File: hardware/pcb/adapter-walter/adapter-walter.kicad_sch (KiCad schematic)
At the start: 4 parts, among them U1 DPT_Walter

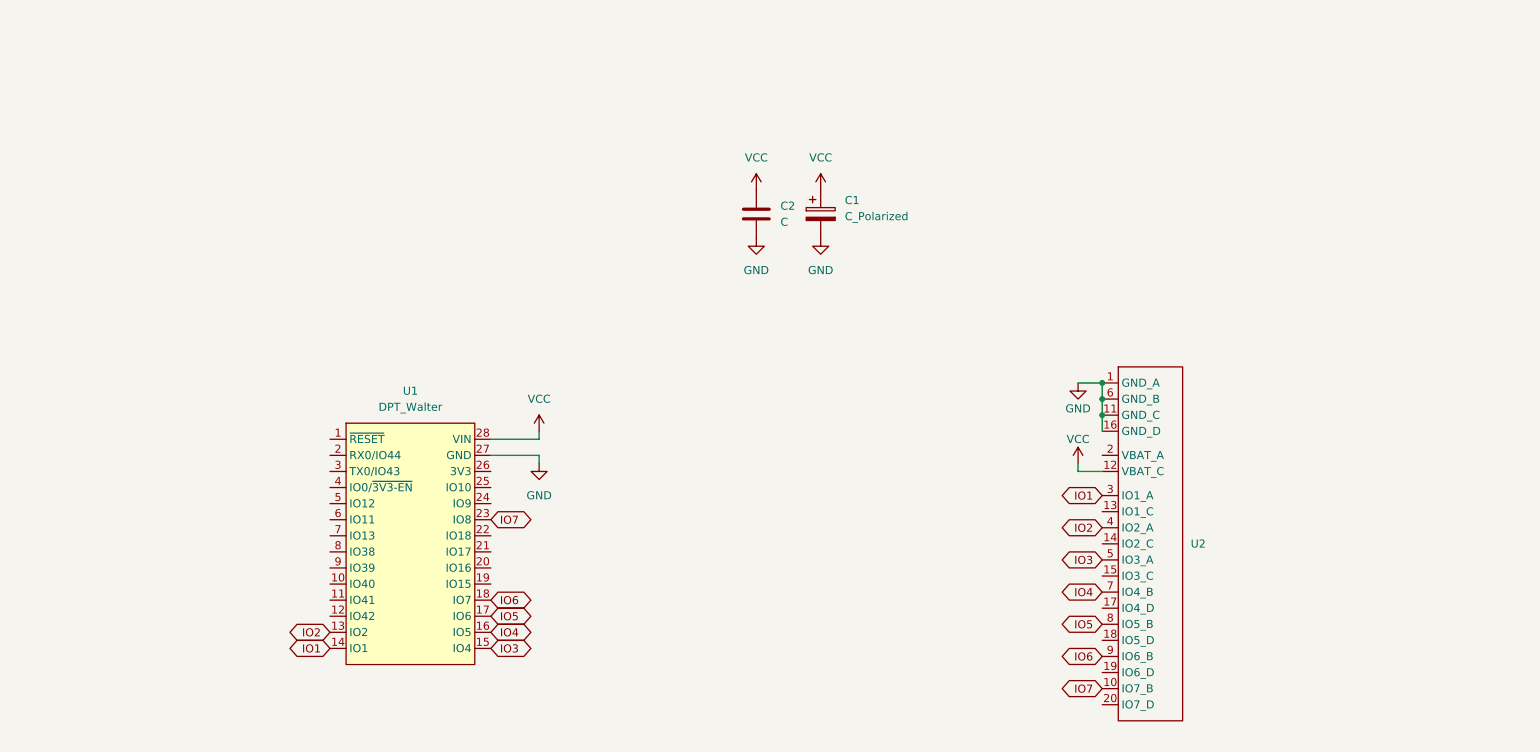
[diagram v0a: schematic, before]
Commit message: Updated Walter adapter schematics
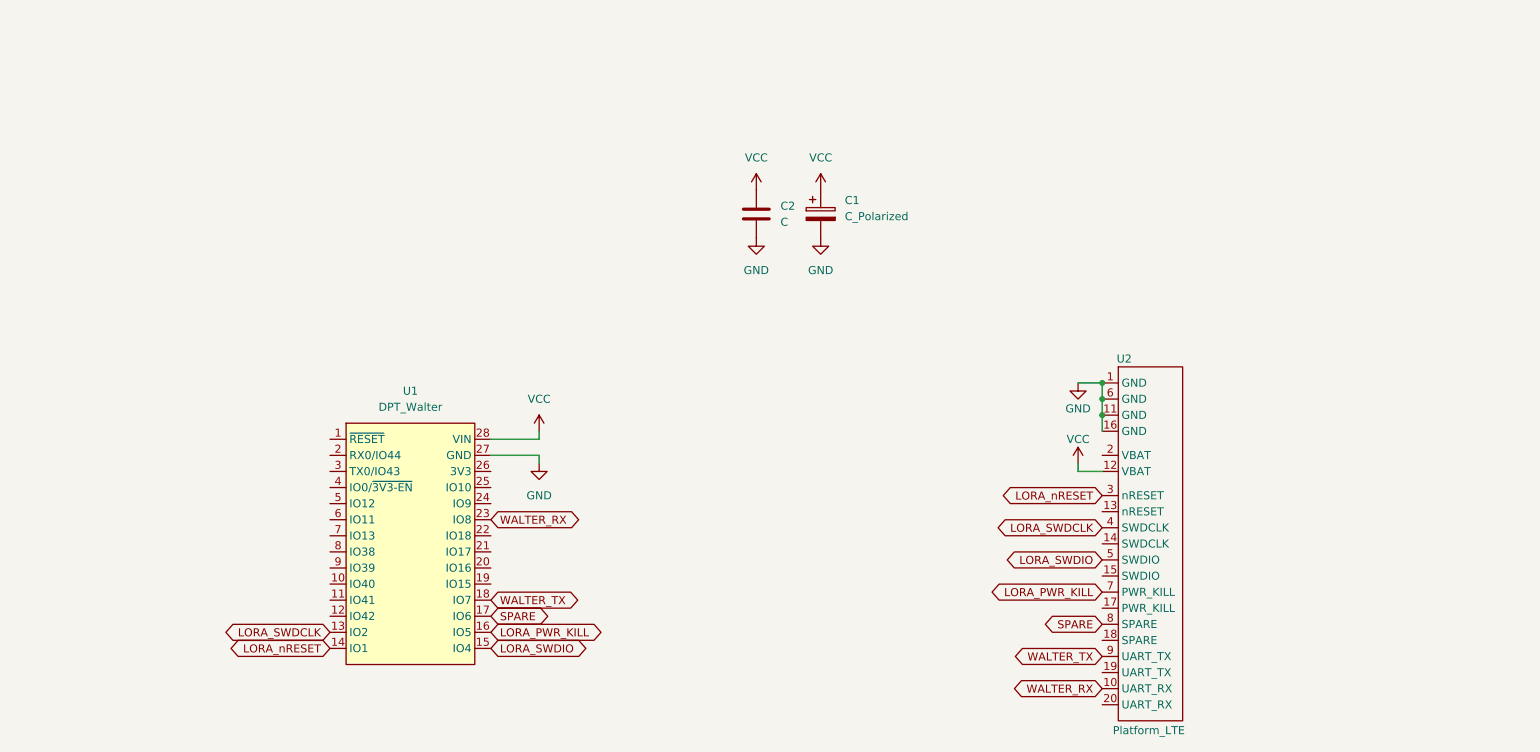
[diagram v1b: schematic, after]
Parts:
- U2: value (none) -> Platform_LTE; symbol TwinOak-standard-repeater-layout:Platform_interface -> TwinOak-standard-repeater-layout:Platform_LTE
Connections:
- net IO1 renamed LORA_nRESET
- net IO2 renamed LORA_SWDCLK
- net IO3 renamed LORA_SWDIO
- net IO4 renamed LORA_PWR_KILL
- net IO5 renamed SPARE
- net IO6 renamed WALTER_TX
- net IO7 renamed WALTER_RX
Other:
- moved on the sheet: U2
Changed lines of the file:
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@@
 		)
 	)
-	(global_label "IO4"
+	(global_label "LORA_PWR_KILL"
 		(shape bidirectional)
 		(at 106.68 118.11 0)
@@
 		)
 	)
-	(global_label "IO7"
+	(global_label "WALTER_RX"
 		(shape bidirectional)
 		(at 106.68 100.33 0)
@@
 		)
 	)
-	(global_label "IO6"
+	(global_label "WALTER_TX"
 		(shape bidirectional)
 		(at 203.2 121.92 180)
@@
 		)
 	)
-	(global_label "IO2"
+	(global_label "LORA_SWDCLK"
 		(shape bidirectional)
 		(at 81.28 118.11 180)
@@
 		)
 	)
-	(global_label "IO1"
+	(global_label "LORA_nRESET"
 		(shape bidirectional)
 		(at 81.28 120.65 180)
@@
 		)
 	)
-	(global_label "IO3"
+	(global_label "LORA_SWDIO"
 		(shape bidirectional)
 		(at 203.2 106.68 180)
@@
 		)
 	)
-	(global_label "IO5"
+	(global_label "SPARE"
 		(shape bidirectional)
 		(at 106.68 115.57 0)
@@
 		)
 	)
-	(global_label "IO6"
+	(global_label "WALTER_TX"
 		(shape bidirectional)
 		(at 106.68 113.03 0)
@@
 		)
 	)
-	(global_label "IO3"
+	(global_label "LORA_SWDIO"
 		(shape bidirectional)
 		(at 106.68 120.65 0)
@@
 		)
 	)
-	(global_label "IO7"
+	(global_label "WALTER_RX"
 		(shape bidirectional)
 		(at 203.2 127 180)
@@
 		)
 	)
-	(global_label "IO1"
+	(global_label "LORA_nRESET"
 		(shape bidirectional)
 		(at 203.2 96.52 180)
@@
 		)
 	)
-	(global_label "IO4"
+	(global_label "LORA_PWR_KILL"
 		(shape bidirectional)
 		(at 203.2 111.76 180)
@@
 		)
 	)
-	(global_label "IO5"
+	(global_label "SPARE"
 		(shape bidirectional)
 		(at 203.2 116.84 180)
@@
 		)
 	)
-	(global_label "IO2"
+	(global_label "LORA_SWDCLK"
 		(shape bidirectional)
 		(at 203.2 101.6 180)
@@
 	)
 	(symbol
-		(lib_id "TwinOak-standard-repeater-layout:Platform_interface")
+		(lib_id "TwinOak-standard-repeater-layout:Platform_LTE")
 		(at 205.74 76.2 0)
 		(unit 1)
@@
 		(in_pos_files yes)
 		(dnp no)
-		(fields_autoplaced yes)
 		(property "Reference" "U2"
-			(at 217.17 104.1399 0)
+			(at 205.486 74.93 0)
 			(show_name no)
 			(do_not_autoplace no)
@@
 			)
 		)
-		(property "Value" ""
-			(at 205.74 76.2 0)
-			(show_name no)
-			(do_not_autoplace no)
+		(property "Value" "Platform_LTE"
+			(at 210.566 133.604 0)
+			(show_name no)
+			(do_not_autoplace no)

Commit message: Cleanup
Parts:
- added SW1: RESET, TwinOak:SW_Push_Kinghelm_KH-6X6X5H-STM, symbol Switch:SW_Push
- C1: value C_Polarized -> 470u 16V; MPN (none) -> Panasonic 16SEPG470M (OS-CON)
- C2: value C -> 10n; MPN (none) -> SR Passives CCT-10N/100V-S
- U1: footprint walter:walter-socket -> TwinOak:walter-socket; symbol walter:DPT_Walter -> TwinOak:DPT_Walter
- U2: footprint TwinOak platform footprints:platform-adapter-footprint -> TwinOak:platform-adapter-footprint; symbol TwinOak-standard-repeater-layout:Platform_LTE -> TwinOak:Platform_LTE
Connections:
- net GND: now also SW1.1
- net WALTER_nRST: now reaches U1.1 (~{RESET})
- net WALTER_nRST: now also SW1.2
- no-connect marks 0 -> 26

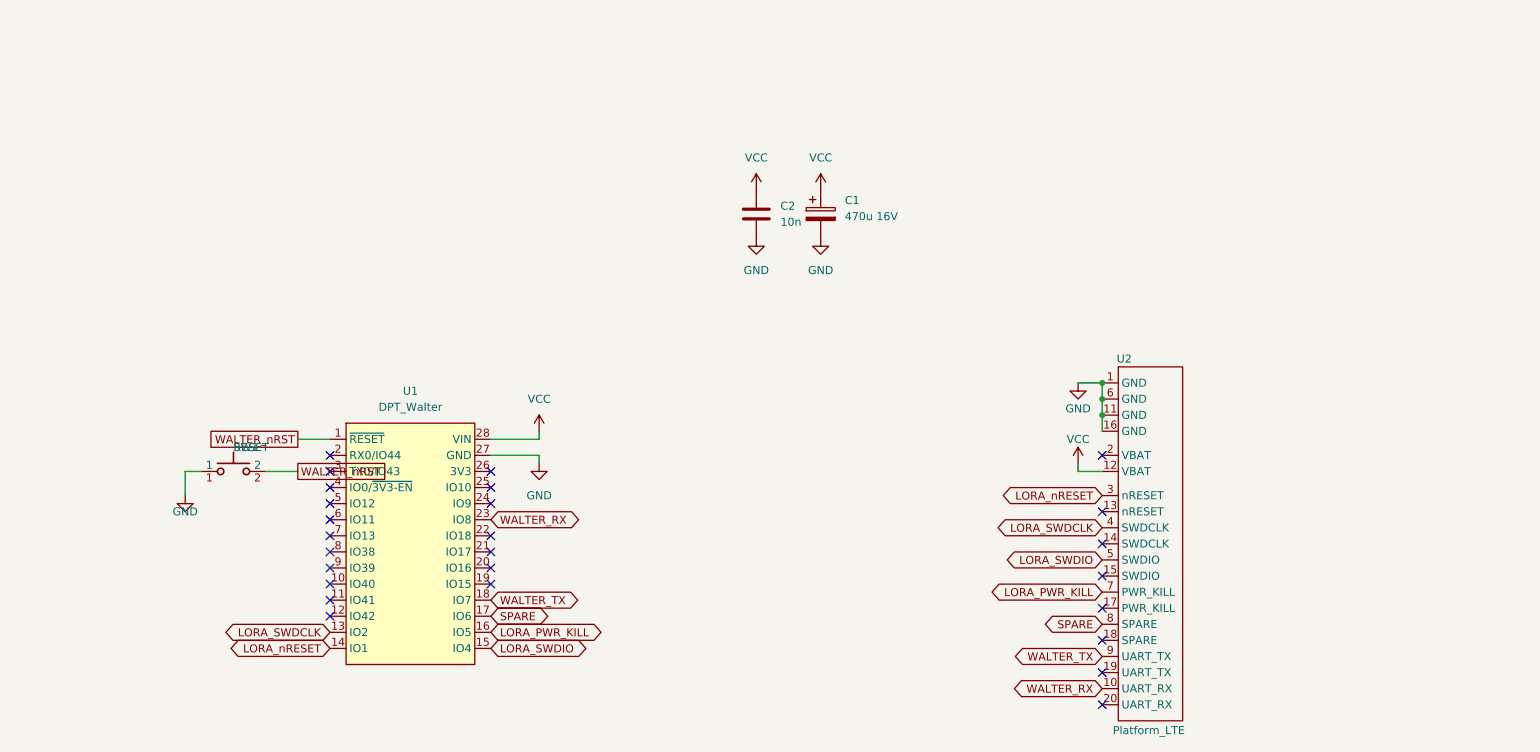
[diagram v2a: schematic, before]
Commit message: Cleanup. Added feedback prevention circuits to Walter adapter
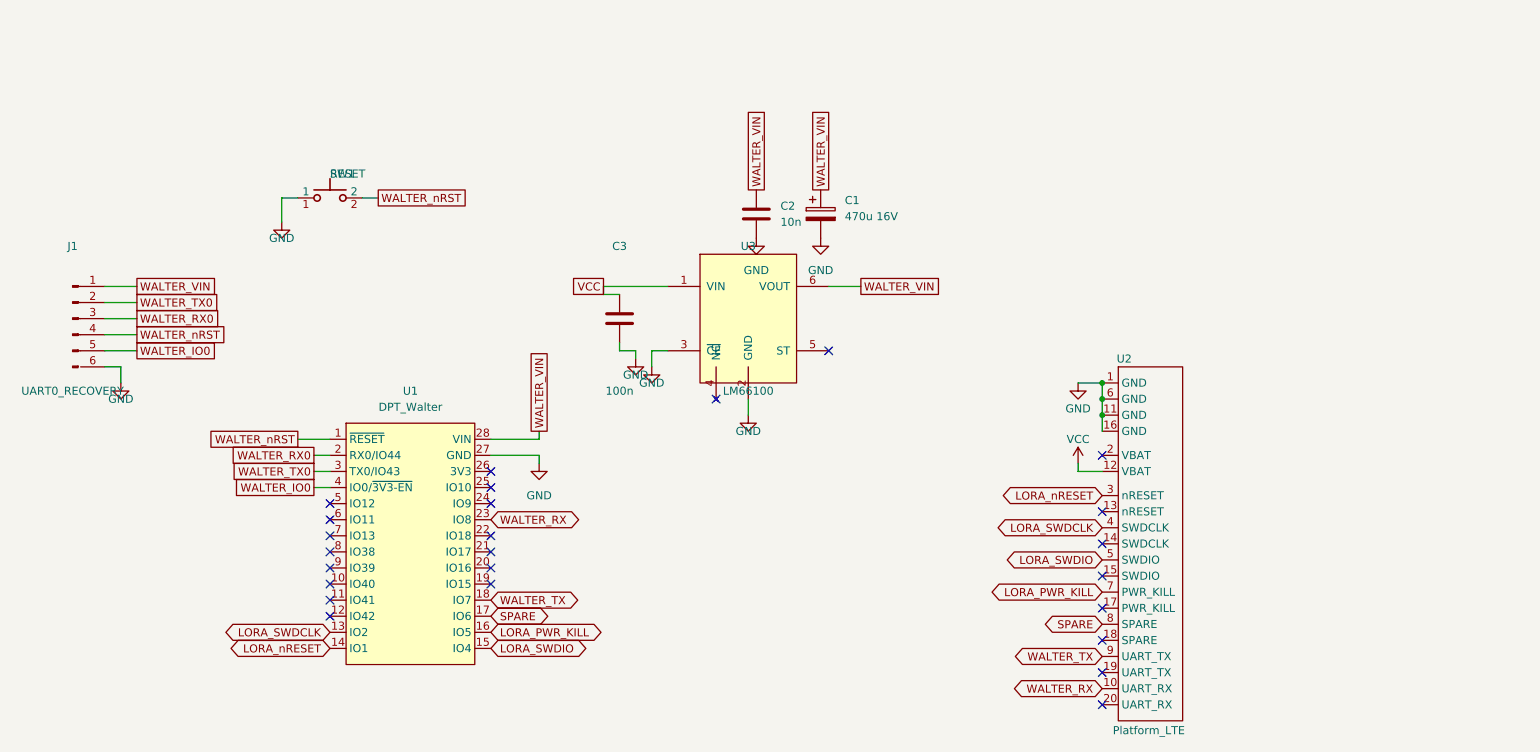
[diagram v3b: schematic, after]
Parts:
- added C3: 100n, Capacitor_SMD:C_0805_2012Metric_Pad1.18x1.45mm_HandSolder, symbol Device:C
- added J1: UART0_RECOVERY, Connector_PinHeader_2.54mm:PinHeader_1x06_P2.54mm_Vertical, symbol Connector:Conn_01x06_Pin
- added U3: LM66100, Package_TO_SOT_SMD:SOT-363_SC-70-6, symbol TwinOak:LM66100
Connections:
- net GND: now also C3.2, J1.6 (Pin_6), U3.2 (GND), U3.3 (~{CE})
- net VCC: now also C3.1, U3.1 (VIN); no longer C1.1, C2.1, U1.28 (VIN)
- net WALTER_nRST: now also J1.4 (Pin_4)
- net WALTER_RX0: now reaches U1.2 (RX0/IO44)
- net WALTER_RX0: now also J1.3 (Pin_3)
- net WALTER_TX0: now reaches U1.3 (TX0/IO43)
- net WALTER_TX0: now also J1.2 (Pin_2)
- net WALTER_IO0: now reaches U1.4 (IO0/~{3V3-EN})
- net WALTER_IO0: now also J1.5 (Pin_5)
- new net WALTER_VIN: C1.1, C2.1, J1.1 (Pin_1), U1.28 (VIN), U3.6 (VOUT)
- no-connect marks 26 -> 25
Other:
- moved on the sheet: SW1

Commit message: Initial routing of walter - Not finished, missing polish
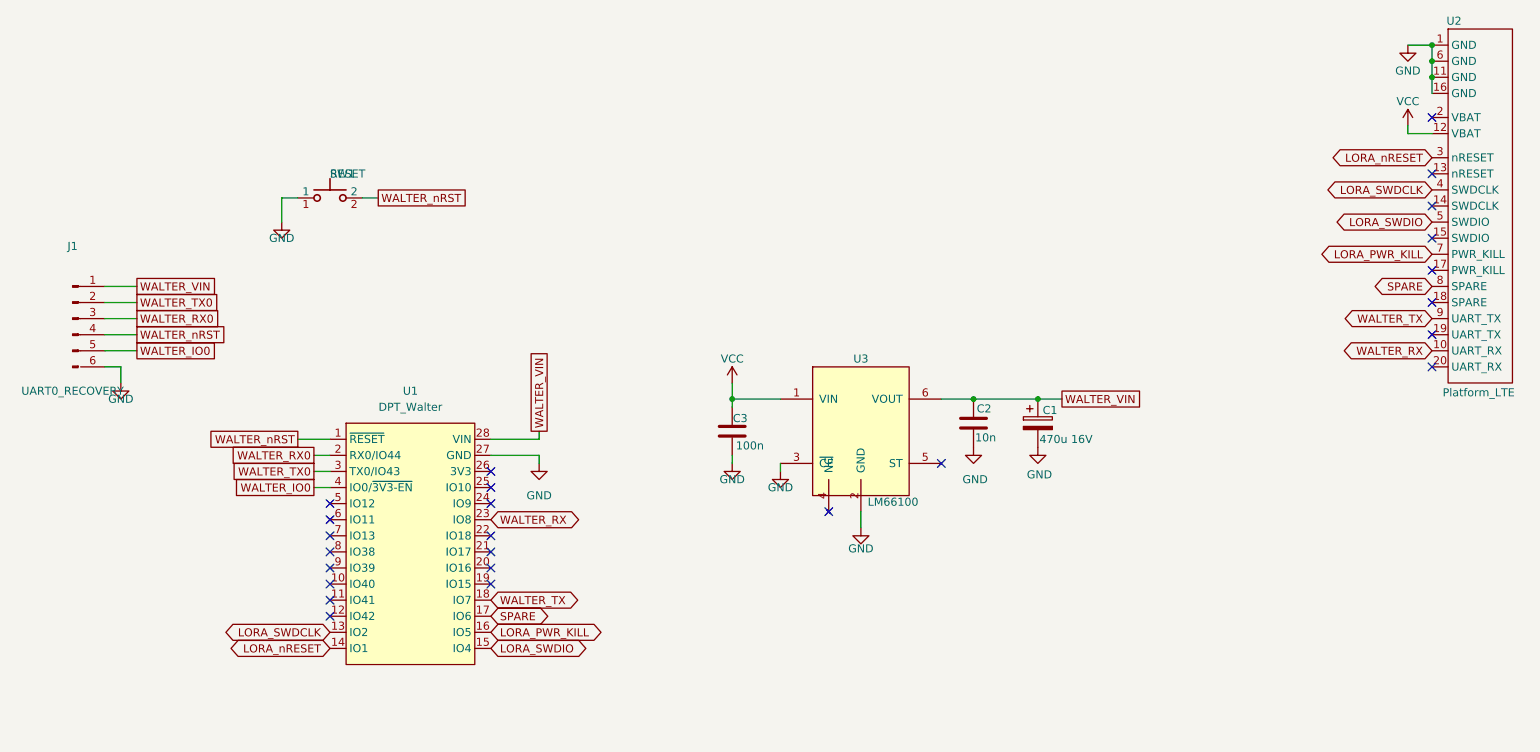
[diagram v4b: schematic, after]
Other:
- moved on the sheet: C1, C2, C3, U2, U3

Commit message: Misc minor updates for production of pcbs
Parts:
- C1, C2, J1: now left out of the parts list
- U1, U2: now not fitted; now left out of the parts list
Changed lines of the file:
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@@
 		(body_style 1)
 		(exclude_from_sim no)
-		(in_bom yes)
-		(on_board yes)
-		(in_pos_files yes)
+		(in_bom no)
+		(on_board yes)
+		(in_pos_files no)
 		(dnp no)
 		(property "Reference" "J1"
@@
 		(body_style 1)
 		(exclude_from_sim no)
-		(in_bom yes)
-		(on_board yes)
-		(in_pos_files yes)
+		(in_bom no)
+		(on_board yes)
+		(in_pos_files no)
 		(dnp no)
 		(property "Reference" "C1"
@@
 		(body_style 1)
 		(exclude_from_sim no)
-		(in_bom yes)
-		(on_board yes)
-		(in_pos_files yes)
-		(dnp no)
+		(in_bom no)
+		(on_board yes)
+		(in_pos_files no)
+		(dnp yes)
 		(property "Reference" "U2"
 			(at 257.556 21.59 0)
@@
 		(body_style 1)
 		(exclude_from_sim no)
-		(in_bom yes)
-		(on_board yes)
-		(in_pos_files yes)
+		(in_bom no)
+		(on_board yes)
+		(in_pos_files no)
 		(dnp no)
 		(property "Reference" "C2"
@@
 		(body_style 1)
 		(exclude_from_sim no)
-		(in_bom yes)
-		(on_board yes)
-		(in_pos_files yes)
-		(dnp no)
+		(in_bom no)
+		(on_board yes)
+		(in_pos_files no)
+		(dnp yes)
 		(fields_autoplaced yes)
 		(property "Reference" "U1"

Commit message: Final PCB adjuments to rev 1.1
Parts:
- U3: LCSC Part # C2869734 -> C2832141
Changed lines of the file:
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@@
 			)
 		)
-		(property "LCSC Part #" "C2869734"
+		(property "LCSC Part #" "C2832141"
 			(at 165.1 86.36 0)
 			(hide yes)

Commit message: Last pre-production updates
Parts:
- U3: FT Rotation Offset (none) -> 90
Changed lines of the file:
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@@
+			)
+		)
+		(property "FT Rotation Offset" "90"
+			(at 165.1 86.36 0)
+			(hide yes)
+			(show_name no)
+			(do_not_autoplace no)
+			(effects
+				(font
+					(size 1.27 1.27)
+				)
 			)
 		)

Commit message: Parts ordered!
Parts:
- C1: LCSC Part # (none) -> C48970577; MPN Panasonic 16SEPG470M (OS-CON) -> Honor Elec RYHT16V470UF8*11 (alt. Panasonic 16SEPG470M)
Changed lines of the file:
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@@
 			)
 		)
-		(property "MPN" "Panasonic 16SEPG470M (OS-CON)"
+		(property "MPN" "Honor Elec RYHT16V470UF8*11 (alt. Panasonic 16SEPG470M)"
 			(at 193.04 85.09 0)
 			(hide yes)
+			(show_name no)
+			(do_not_autoplace no)
+			(effects
+				(font
+					(size 1.27 1.27)
+				)
+			)
+		)
+		(property "LCSC Part #" "C48970577"
+			(at 193.04 85.09 0)
+			(hide yes)
